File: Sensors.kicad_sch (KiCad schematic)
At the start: 13 parts, among them J1 BM04B-GHS-TBT, J2 BM02B-GHS-TBT, J3 BM02B-GHS-TBT, J4 BM02B-GHS-TBT, J5 BM02B-GHS-TBT, J6 Conn_01x03_Pin, J7 BM04B-GHS-TBT, Q1 PNP

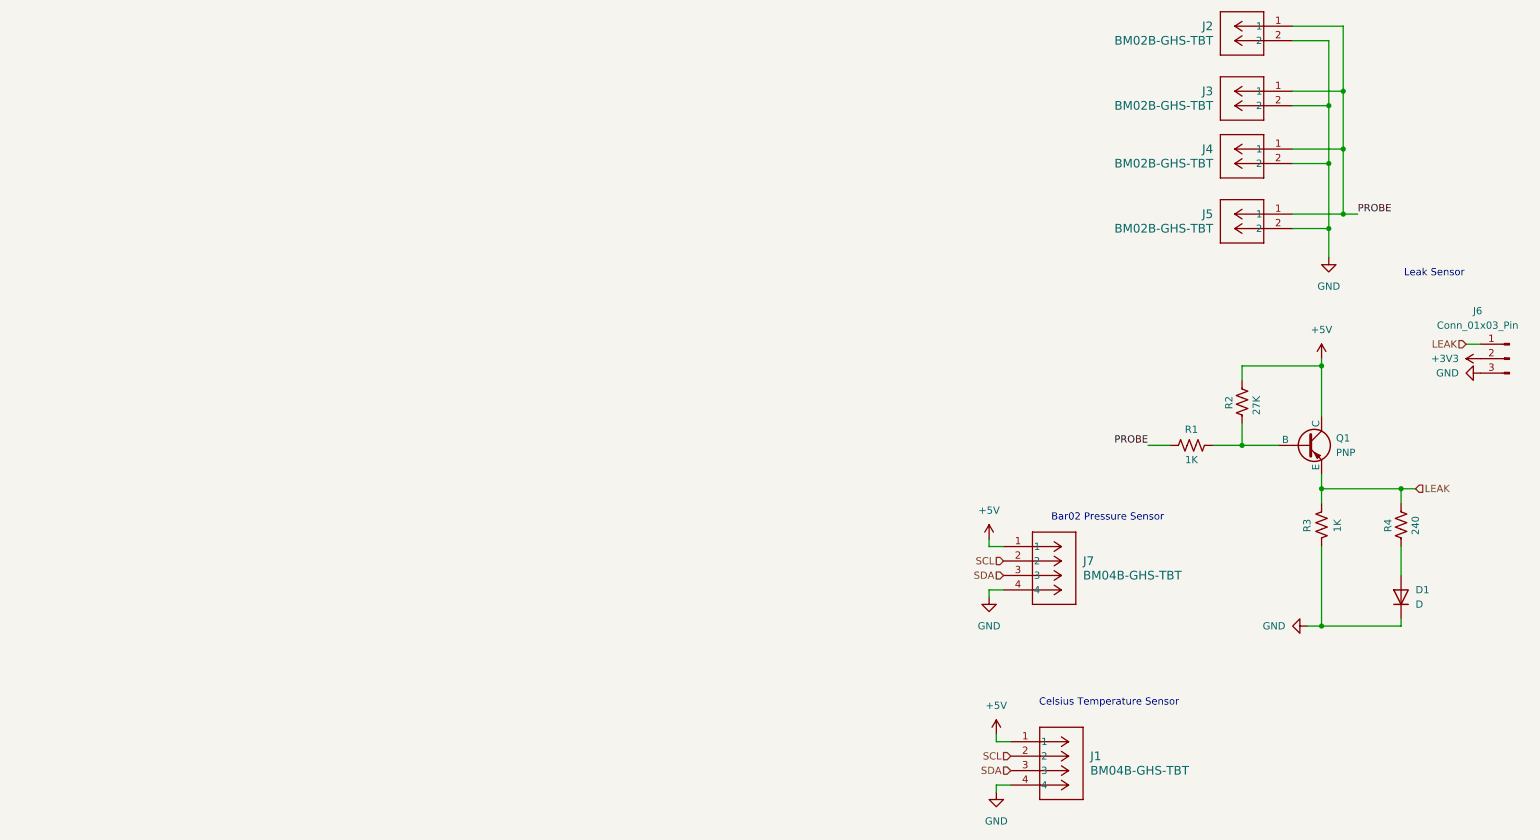
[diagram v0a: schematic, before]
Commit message: Added New Libraries and Schematic Updates
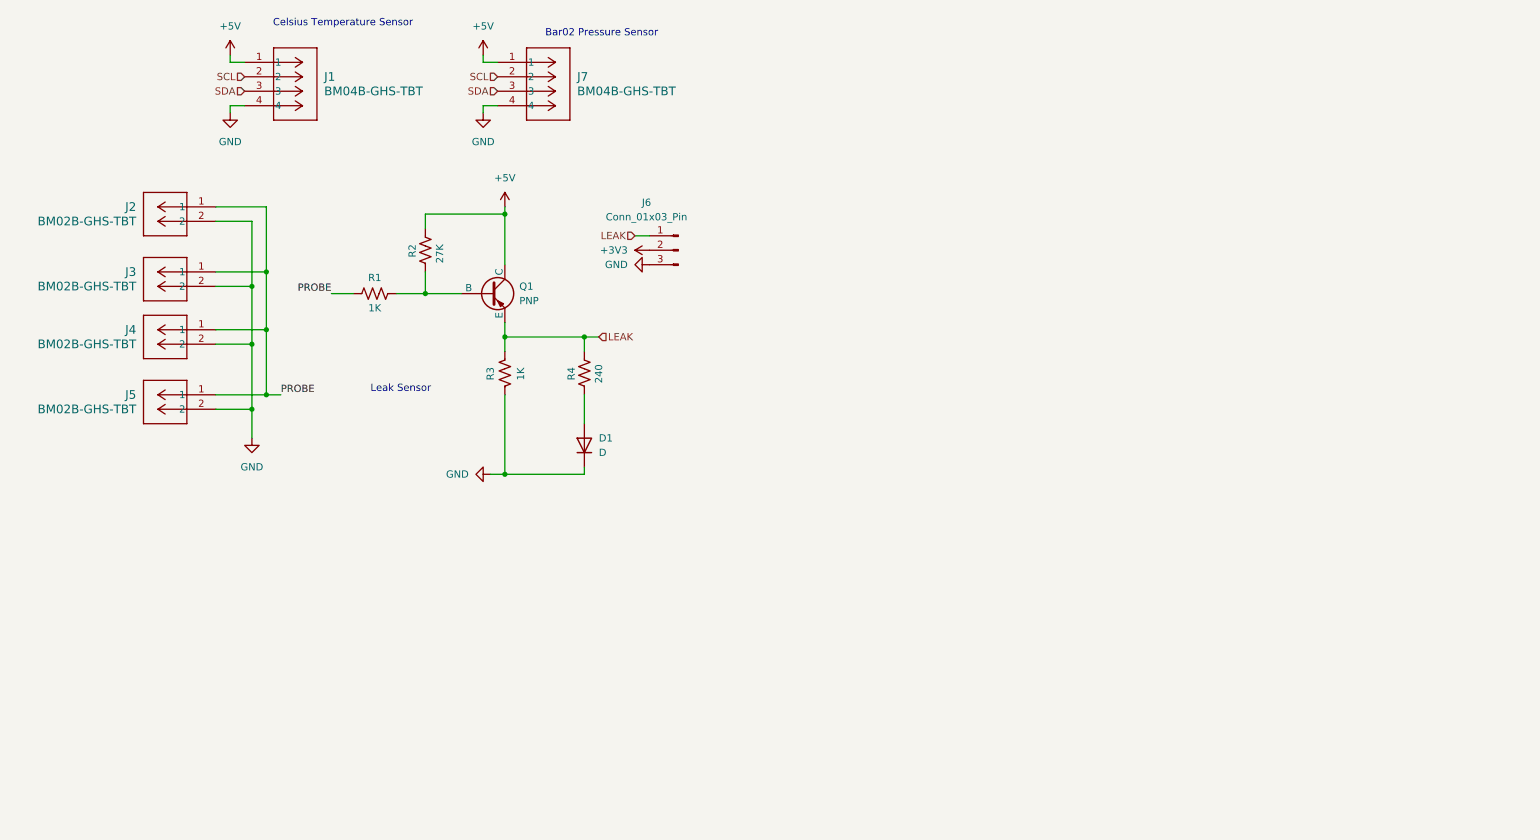
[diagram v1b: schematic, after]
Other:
- moved on the sheet: D1, J1, J2, J3, J4, J5, J6, J7, Q1, R1, R2, R3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

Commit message: Root Update and Adding ISO Pt1
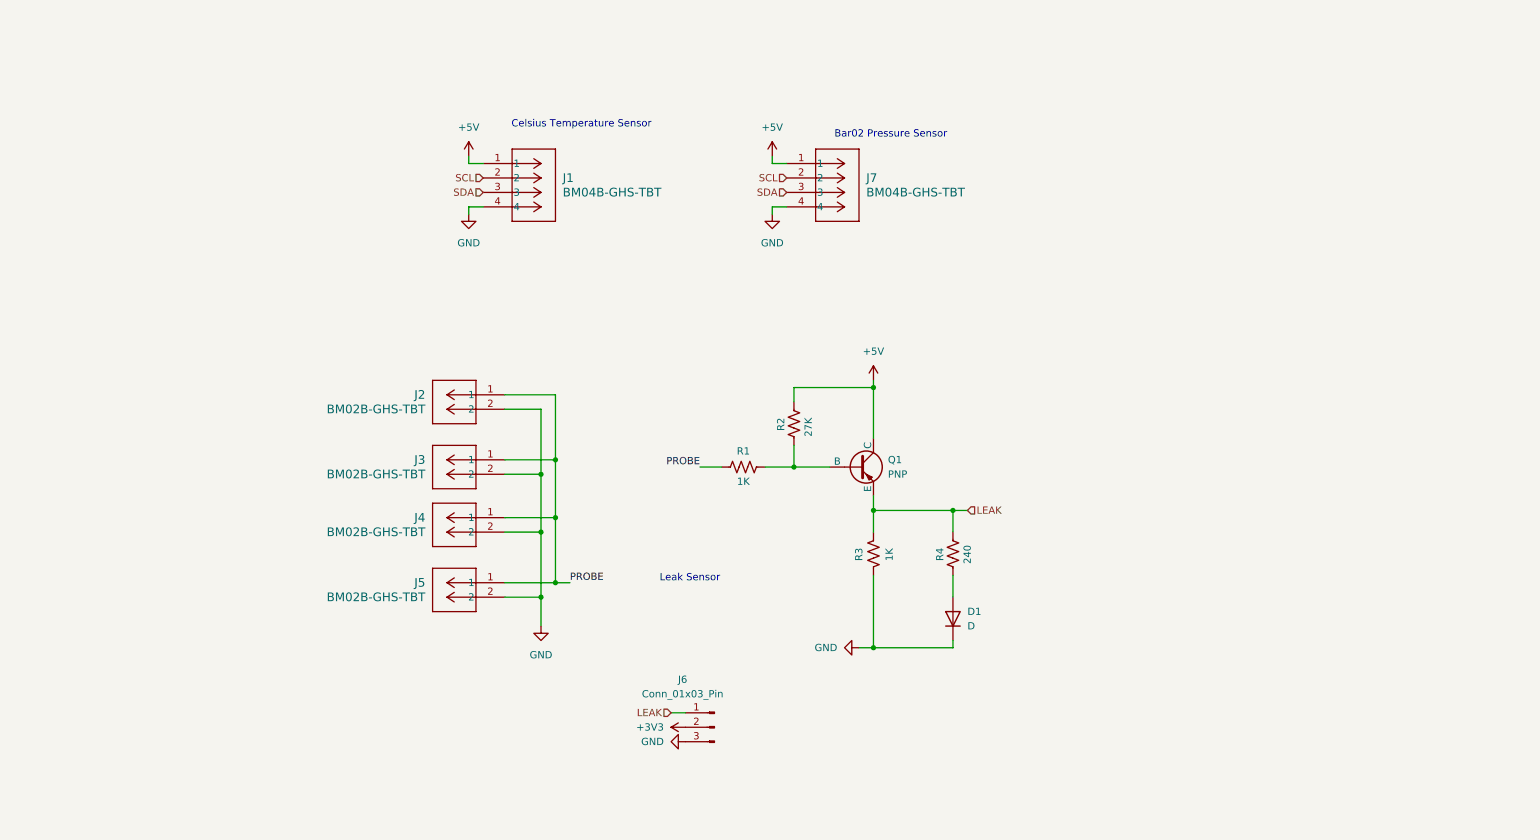
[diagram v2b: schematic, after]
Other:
- moved on the sheet: D1, J1, J2, J3, J4, J5, J6, J7, Q1, R1, R2, R3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

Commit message: Finalizing Schematic
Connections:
- net +3V3: now also J1.1, J7.1
- net +5V: no longer J1.1, J7.1
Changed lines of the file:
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@@
 	(text "Leak Sensor\n"
 		(exclude_from_sim no)
-		(at 135.382 118.618 0)
+		(at 138.938 118.364 0)
 		(effects
 			(font
@@
 	)
 	(symbol
-		(lib_id "power:+5V")
-		(at 96.52 44.45 0)
-		(unit 1)
-		(exclude_from_sim no)
-		(in_bom yes)
-		(on_board yes)
-		(dnp no)
-		(fields_autoplaced yes)
-		(property "Reference" "#PWR03"
-			(at 96.52 48.26 0)
-			(effects
-				(font
-					(size 1.27 1.27)
-				)
-				(hide yes)
-			)
-		)
-		(property "Value" "+5V"
-			(at 96.52 39.37 0)
-			(effects
-				(font
-					(size 1.27 1.27)
-				)
-			)
-		)
-		(property "Footprint" ""
-			(at 96.52 44.45 0)
-			(effects
-				(font
-					(size 1.27 1.27)
-				)
-				(hide yes)
-			)
-		)
-		(property "Datasheet" ""
-			(at 96.52 44.45 0)
-			(effects
-				(font
-					(size 1.27 1.27)
-				)
-				(hide yes)
-			)
-		)
-		(property "Description" "Power symbol creates a global label with name \"+5V\""
-			(at 96.52 44.45 0)
-			(effects
-				(font
-					(size 1.27 1.27)
-				)
-				(hide yes)
-			)
-		)
-		(pin "1"
-		)
-		(instances
-			(project "X17_Pi_Shield"
-				(path "/9eec1df9-cfd8-4f98-afed-20048a6985e2/ac9ebbc7-7dce-474a-a1ee-16705e6debeb"
-					(reference "#PWR03")
-					(unit 1)
-				)
-			)
-		)
-	)
-	(symbol
 		(lib_id "Simulation_SPICE:PNP")
 		(at 165.1 99.06 0)
@@
 	)
 	(symbol
-		(lib_id "power:+5V")
-		(at 149.86 44.45 0)
-		(unit 1)
-		(exclude_from_sim no)
-		(in_bom yes)
-		(on_board yes)
-		(dnp no)
-		(fields_autoplaced yes)
-		(property "Reference" "#PWR01"
-			(at 149.86 48.26 0)
-			(effects
-				(font
-					(size 1.27 1.27)
-				)
-				(hide yes)
-			)
-		)
-		(property "Value" "+5V"
-			(at 149.86 39.37 0)
-			(effects
-				(font
-					(size 1.27 1.27)
-				)
-			)
-		)
-		(property "Footprint" ""
-			(at 149.86 44.45 0)
-			(effects
-				(font
-					(size 1.27 1.27)
-				)
-				(hide yes)
-			)
-		)
-		(property "Datasheet" ""
-			(at 149.86 44.45 0)
-			(effects
-				(font
-					(size 1.27 1.27)
-				)
-				(hide yes)
-			)
-		)
-		(property "Description" "Power symbol creates a global label with name \"+5V\""
-			(at 149.86 44.45 0)
-			(effects
-				(font
-					(size 1.27 1.27)
-				)
-				(hide yes)
-			)
-		)
-		(pin "1"
-		)
-		(instances
-			(project ""
-				(path "/9eec1df9-cfd8-4f98-afed-20048a6985e2/ac9ebbc7-7dce-474a-a1ee-16705e6debeb"
-					(reference "#PWR01")
-					(unit 1)
-				)
-			)
-		)
-	)
-	(symbol
 		(lib_id "leak_probe_connector:BM02B-GHS-TBT")
 		(at 102.87 119.38 0)
@@
 	)
 	(symbol
+		(lib_id "power:+3V3")
+		(at 149.86 44.45 0)
+		(unit 1)
+		(exclude_from_sim no)
+		(in_bom yes)
+		(on_board yes)
+		(dnp no)
+		(fields_autoplaced yes)
+		(property "Reference" "#PWR01"
+			(at 149.86 48.26 0)
+			(effects
+				(font
+					(size 1.27 1.27)
+				)
+				(hide yes)
+			)
+		)
+		(property "Value" "+3V3"
+			(at 149.86 39.37 0)
+			(effects
+				(font
+					(size 1.27 1.27)
+				)
+			)
+		)
+		(property "Footprint" ""
+			(at 149.86 44.45 0)
+			(effects
+				(font
+					(size 1.27 1.27)
+				)
+				(hide yes)
+			)
+		)
+		(property "Datasheet" ""
+			(at 149.86 44.45 0)
+			(effects
+				(font
+					(size 1.27 1.27)
+				)
+				(hide yes)
+			)
+		)
+		(property "Description" "Power symbol creates a global label with name \"+3V3\""
+			(at 149.86 44.45 0)
+			(effects
+				(font
+					(size 1.27 1.27)
+				)
+				(hide yes)
+			)
+		)
+		(pin "1"
+		)
+		(instances
+			(project "X17_Pi_Shield"
+				(path "/9eec1df9-cfd8-4f98-afed-20048a6985e2/ac9ebbc7-7dce-474a-a1ee-16705e6debeb"
+					(reference "#PWR01")
+					(unit 1)
+				)
+			)
+		)
+	)
+	(symbol
 		(lib_id "Device:R_US")
 		(at 144.78 99.06 90)
@@
 					(unit 1)
 				)
+			)
+		)
+	)
+	(symbol
+		(lib_id "power:+3V3")
+		(at 96.52 44.45 0)
+		(unit 1)
+		(exclude_from_sim no)
+		(in_bom yes)
+		(on_board yes)
+		(dnp no)
+		(fields_autoplaced yes)
+		(property "Reference" "#PWR062"
+			(at 96.52 48.26 0)
+			(effects
+				(font
+					(size 1.27 1.27)
+				)
+				(hide yes)
+			)
+		)
+		(property "Value" "+3V3"
+			(at 96.52 39.37 0)
+			(effects
+				(font
+					(size 1.27 1.27)
+				)
+			)
+		)
+		(property "Footprint" ""
+			(at 96.52 44.45 0)
+			(effects
+				(font
+					(size 1.27 1.27)
+				)
+				(hide yes)
+			)
+		)
+		(property "Datasheet" ""
+			(at 96.52 44.45 0)
+			(effects
+				(font
+					(size 1.27 1.27)
+				)
+				(hide yes)
+			)
+		)
+		(property "Description" "Power symbol creates a global label with name \"+3V3\""
+			(at 96.52 44.45 0)
+			(effects
+				(font
+					(size 1.27 1.27)
+				)
+				(hide yes)
+			)
+		)
+		(pin "1"
+		)
+		(instances
+			(project ""
+				(path "/9eec1df9-cfd8-4f98-afed-20048a6985e2/ac9ebbc7-7dce-474a-a1ee-16705e6debeb"
+					(reference "#PWR062")
+					(unit 1)
+				)

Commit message: Final Schematic Update
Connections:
- net +3V3: now also Q1.3 (E), R2.2
- net LEAK: now also Q1.1 (C); no longer Q1.3 (E)
- removed net +5V: Q1.1 (C), R2.2
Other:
- moved on the sheet: D1, J1, J2, J3, J4, J5, J6, J7, Q1, R1, R2, R3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

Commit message: Pre-Toolbox Final
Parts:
- J2, J3, J4, J5: footprint CONN_BM02B-GHS-TBT_JST -> leak_footprint:CONN_BM02B-GHS-TBT_JST
- J7: footprint CONN_BM04B-GHS-TBT_JST -> Connector_JST:JST_GH_BM04B-GHS-TBT_1x04-1MP_P1.25mm_Vertical
- R1, R2, R3, R4: footprint (none) -> Resistor_SMD:R_0805_2012Metric_Pad1.20x1.40mm_HandSolder
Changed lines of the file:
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@@
 			)
 		)
-		(property "Footprint" "CONN_BM02B-GHS-TBT_JST"
+		(property "Footprint" "leak_footprint:CONN_BM02B-GHS-TBT_JST"
 			(at 66.04 88.9 0)
 			(effects
@@
 			)
 		)
-		(property "Footprint" ""
+		(property "Footprint" "Resistor_SMD:R_0805_2012Metric_Pad1.20x1.40mm_HandSolder"
 			(at 145.796 105.664 90)
 			(effects
@@
 			)
 		)
-		(property "Footprint" "CONN_BM02B-GHS-TBT_JST"
+		(property "Footprint" "leak_footprint:CONN_BM02B-GHS-TBT_JST"
 			(at 66.04 110.49 0)
 			(effects
@@
 			)
 		)
-		(property "Footprint" ""
+		(property "Footprint" "Resistor_SMD:R_0805_2012Metric_Pad1.20x1.40mm_HandSolder"
 			(at 131.826 105.156 90)
 			(effects
@@
 			)
 		)
-		(property "Footprint" ""
+		(property "Footprint" "Resistor_SMD:R_0805_2012Metric_Pad1.20x1.40mm_HandSolder"
 			(at 108.204 89.154 90)
 			(effects
@@
 			)
 		)
-		(property "Footprint" ""
+		(property "Footprint" "Resistor_SMD:R_0805_2012Metric_Pad1.20x1.40mm_HandSolder"
 			(at 115.824 82.296 90)
 			(effects
@@
 			)
 		)
-		(property "Footprint" "CONN_BM02B-GHS-TBT_JST"
+		(property "Footprint" "leak_footprint:CONN_BM02B-GHS-TBT_JST"
 			(at 66.04 99.06 0)
 			(effects
@@
 			)
 		)
-		(property "Footprint" "CONN_BM02B-GHS-TBT_JST"
+		(property "Footprint" "leak_footprint:CONN_BM02B-GHS-TBT_JST"
 			(at 66.04 77.47 0)
 			(effects
@@
 			)
 		)
-		(property "Footprint" "CONN_BM04B-GHS-TBT_JST"
+		(property "Footprint" "Connector_JST:JST_GH_BM04B-GHS-TBT_1x04-1MP_P1.25mm_Vertical"
 			(at 213.36 119.38 0)
 			(effects

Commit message: Finalized Footprints
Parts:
- removed D1: D, symbol Device:D
- removed Q1: PNP, symbol Simulation_SPICE:PNP
- added D1: LED, LED_SMD:LED_0805_2012Metric_Pad1.15x1.40mm_HandSolder, symbol Device:LED
- added U6: MMBT3906LT3G, MMBT3906LT3G:SOT-23-3_1P4X3P040_ONS, symbol MMBT3906LT3G:MMBT3906LT3G
- R1, R2, R3, R4: footprint Resistor_SMD:R_0805_2012Metric_Pad1.20x1.40mm_HandSolder -> Resistor_SMD:R_0603_1608Metric_Pad0.98x0.95mm_HandSolder
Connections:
- net +3V3: now also U6.2 (EMITTER)
- net GND: now also D1.1 (K)
- net LEAK: now also U6.3 (COLLECTOR)
- net at R1.2, R2.1: now also U6.1 (BASE)
- net at R4.2: now also D1.2 (A)
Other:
- note added: "PNP Transistor"
- moved on the sheet: J6, J7, R2, R3, R4
